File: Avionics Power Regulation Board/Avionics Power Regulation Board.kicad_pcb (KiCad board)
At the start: 2 copper layers, 127.4 x 80.5 mm, 56 parts, among them J1 Conn_01x05_Socket, Q1 NMOS, Q2 PMOS, Q3 NMOS, SW1 SW_Push, U1 LM2576HVS-5, U2 BQ76920PW, U4 TPS61085DGK

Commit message: Extra touches
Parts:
- moved BT1 72.2 mm to (62.8, 57.6)
- moved C3 72.2 mm to (144.0, 49.2)
- moved C5 72.2 mm to (132.9, 49.2)
- moved CAP1 72.2 mm to (108.5, 58.9)
- moved CBY1 72.2 mm to (120.3, 69.8)
- moved CC1 72.2 mm to (115.8, 58.4)
- moved CC5 72.2 mm to (115.8, 35.2)
- moved CIN1 72.2 mm to (133.4, 65.9)
- moved CSS1 72.2 mm to (125.6, 66.0)
- moved Ccomp1 72.2 mm to (115.8, 63.5)
- moved Cout1 72.2 mm to (106.6, 74.0)
- moved Cout2 72.2 mm to (106.8, 80.3)
- moved D1 72.2 mm to (143.7, 71.4)
- moved D2 72.2 mm to (108.8, 85.4)
- moved H1 72.2 mm to (145.4, 95.0)
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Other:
- board text added: "AIAA Fresno NASA SLI (2024-25) Avionics Power Regulation Board Designed by Carlos Cortes Version 1.0"

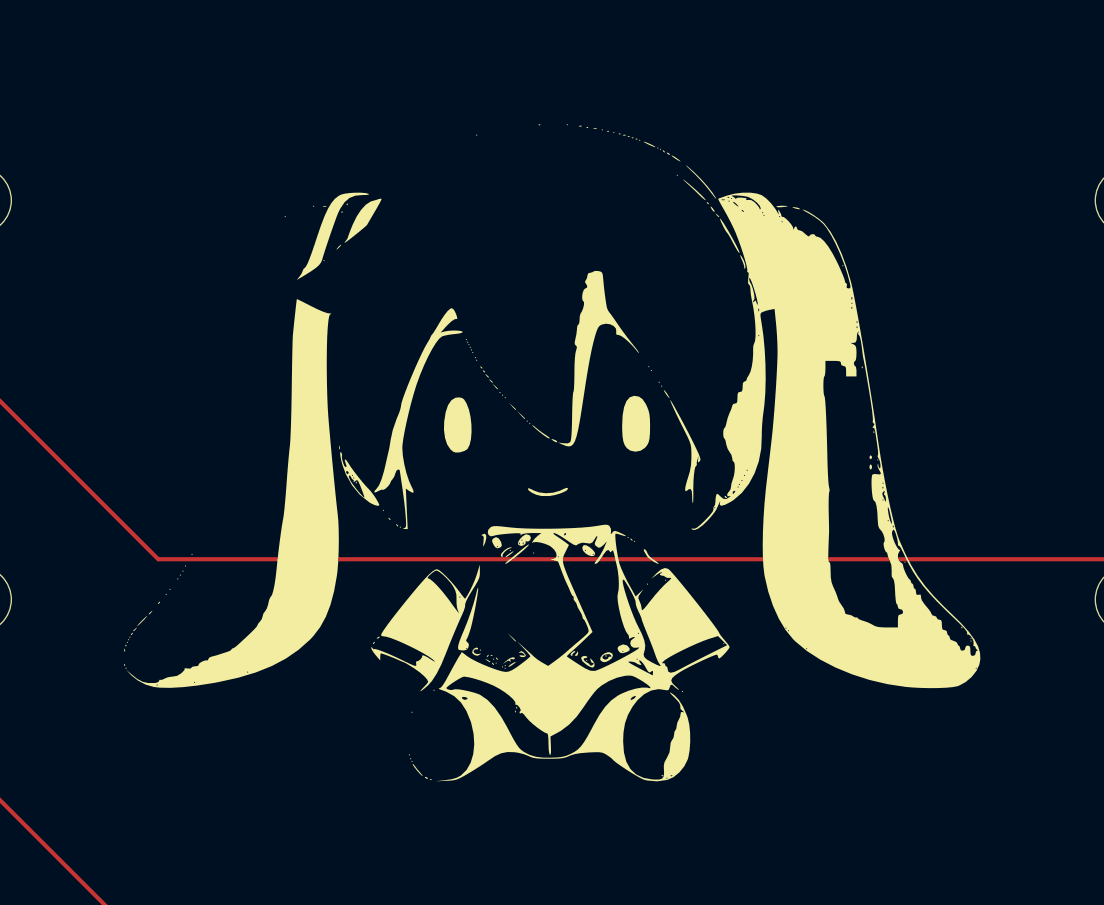
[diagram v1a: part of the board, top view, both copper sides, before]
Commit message: Adding to the Avionics Sensors Board
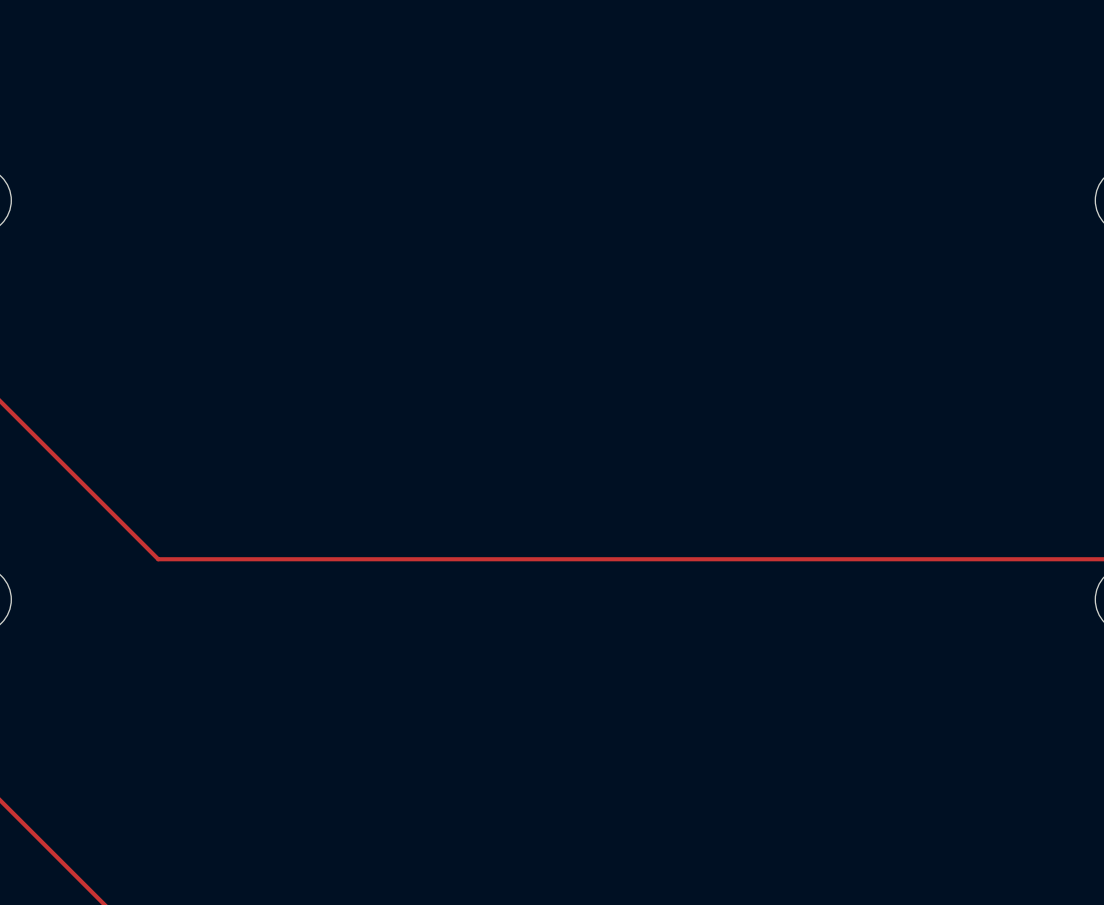
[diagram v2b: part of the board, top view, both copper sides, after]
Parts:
- removed the G*** at (62.4, 58.1)
